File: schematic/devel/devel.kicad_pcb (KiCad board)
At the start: 4 copper layers, 63 x 40 mm, 51 parts, among them J1 CONN_PWR, J2 CONN_X1, J3 CONN_Y2, J4 CONN_X2, J5 CONN_Y1, M2 MountingHole_2.2mm_M2, U1 LM317_SOT223, U2 LM337_SOT223, U3 REF5010IDGK, U4 OPA4197

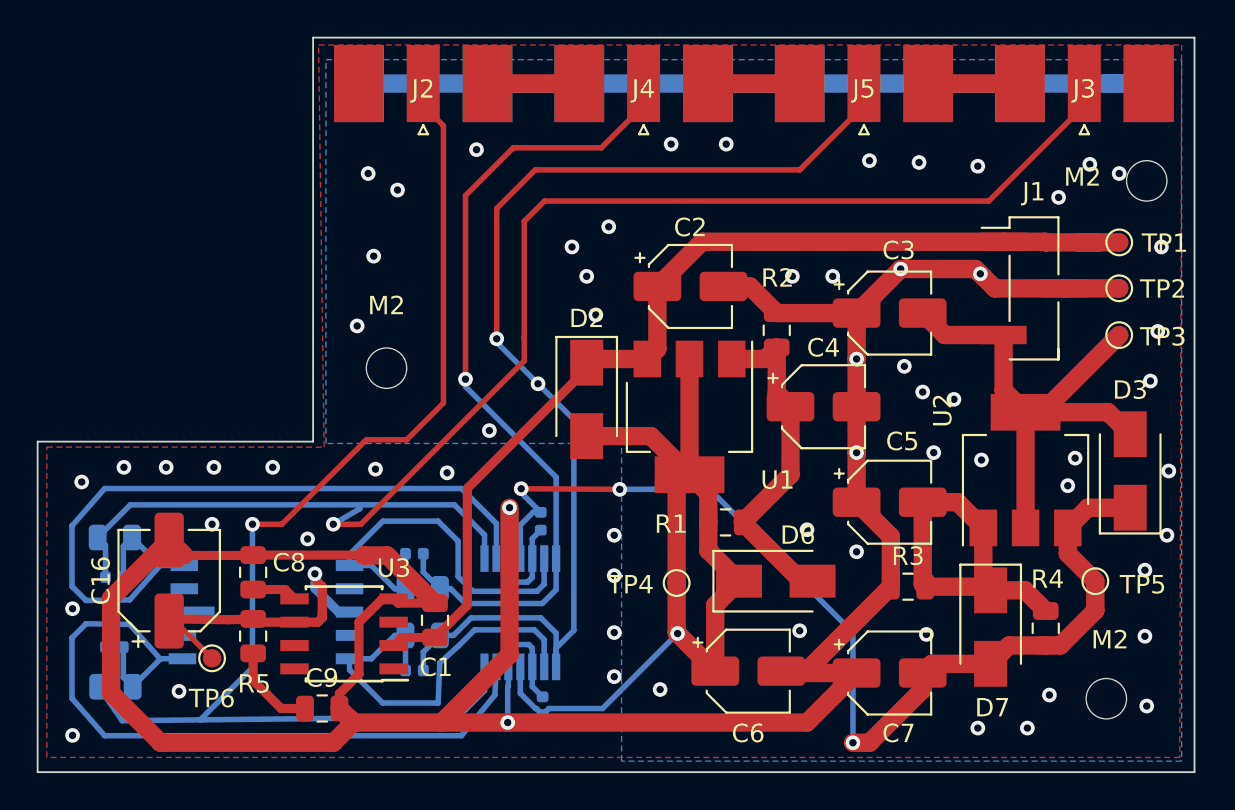
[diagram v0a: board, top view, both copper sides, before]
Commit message: realigned vias, added silk labels
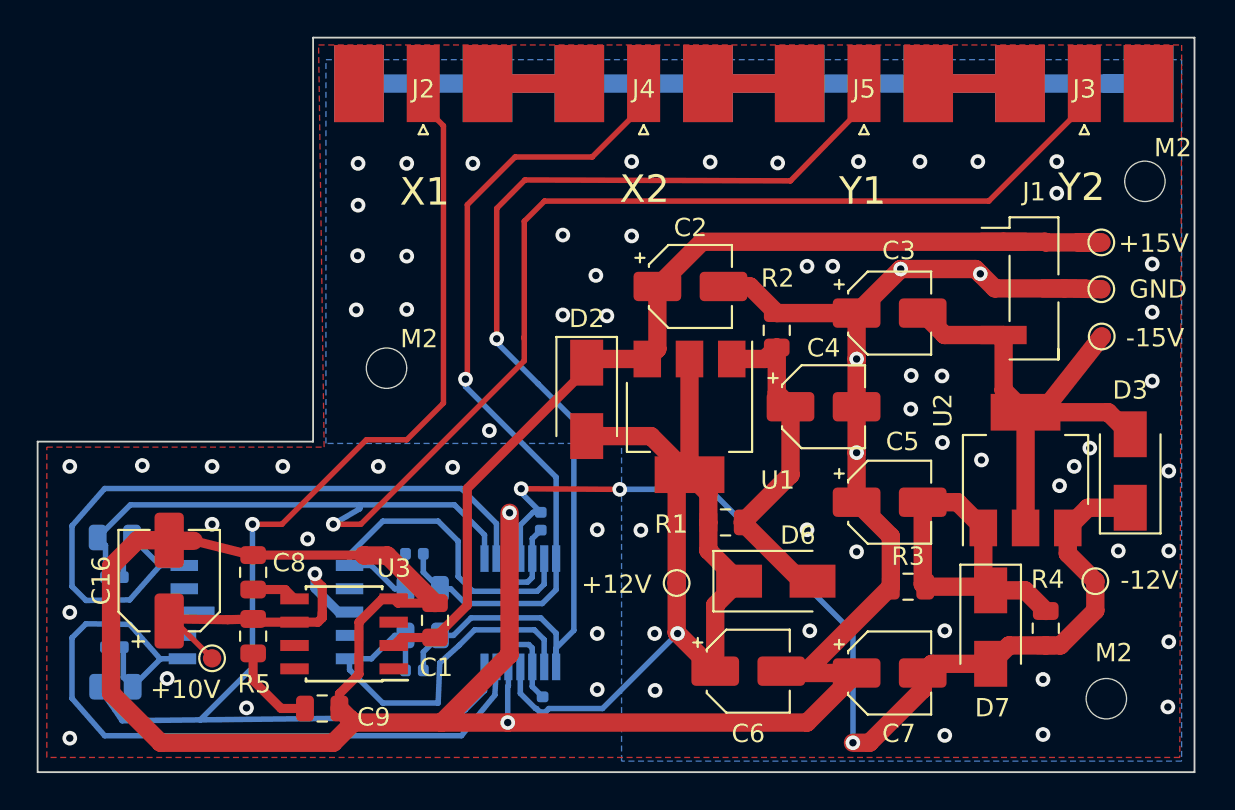
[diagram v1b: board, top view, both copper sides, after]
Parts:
- +10V: renamed from TP6; value TestPoint -> +10V
- +12V: renamed from TP4; value TestPoint -> +12V
- +15V: renamed from TP1; value TestPoint -> +15V
- -12V: renamed from TP5; value TestPoint -> -12V
- -15V: renamed from TP3; value TestPoint -> -15V
- C10, C11: value 0.1u -> 100n
- GND: renamed from TP2; value TestPoint -> GND
- moved GND 0.98 mm to (142.9, 113.7)
- moved +15V 0.97 mm to (142.9, 111.2)
- moved -15V 0.95 mm to (142.9, 116.3)
- moved M2 0.10 mm to (145.3, 107.8)
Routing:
- net +15V: track 55.7 -> 54.7 mm
- net -15V: track 28.9 -> 28.2 mm
- net GND: track 221.4 -> 221.0 mm, vias 64 -> 71
- net Net-(C15-Pad2): track 61.8 -> 61.9 mm, vias 2 -> 1
- net (no net): vias 1 -> 0
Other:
- board text added: "X1"
- board text added: "X2"
- board text added: "Y1"
- board text added: "Y2"
